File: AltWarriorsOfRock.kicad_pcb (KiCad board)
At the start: 2 copper layers, 33 x 90.5 mm, 40 parts, among them J1 Fret Board, J2 PM20205HBDN, J3 PM20203HBDN, J4 USB4930-00-A_REVA, J5 Debug, SW3 1825910-6, SW4 1825910-6, U1 ESP32-S3-WROOM-1, U2 AMS1117-3.3

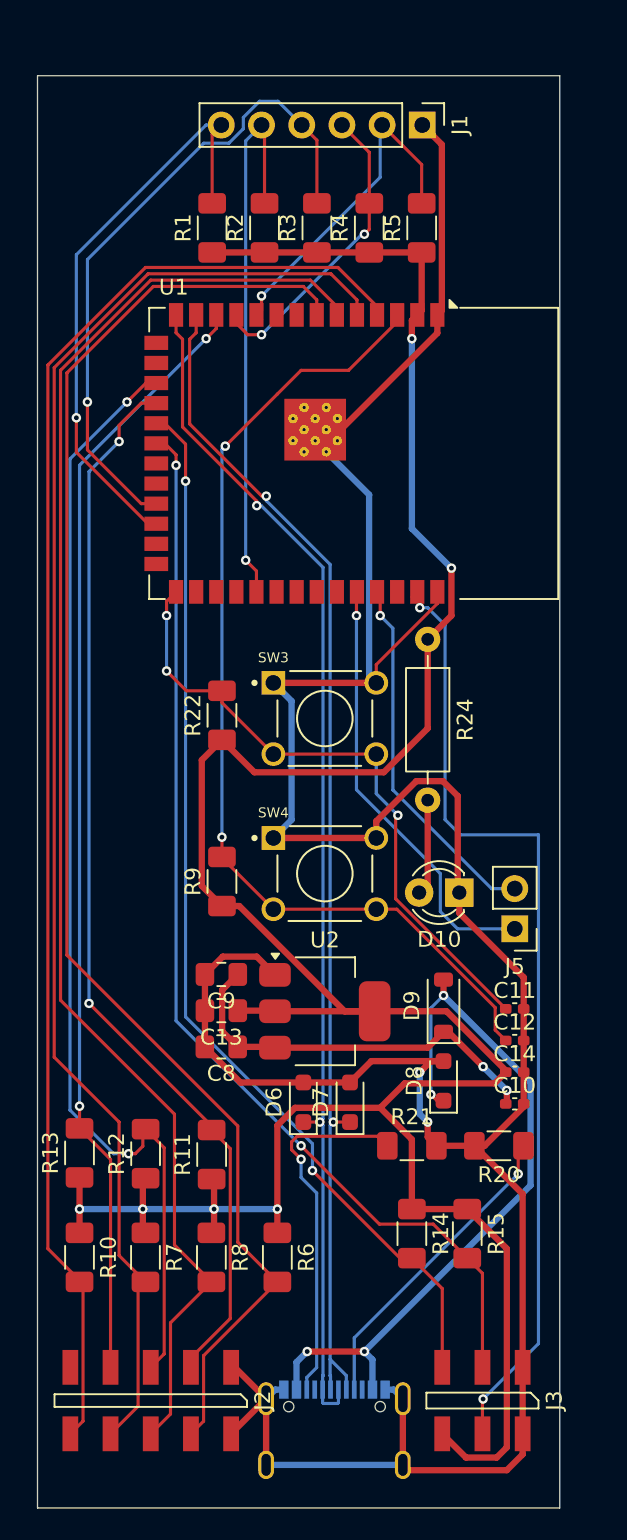
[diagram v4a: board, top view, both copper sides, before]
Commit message: Redo layout with all components topside
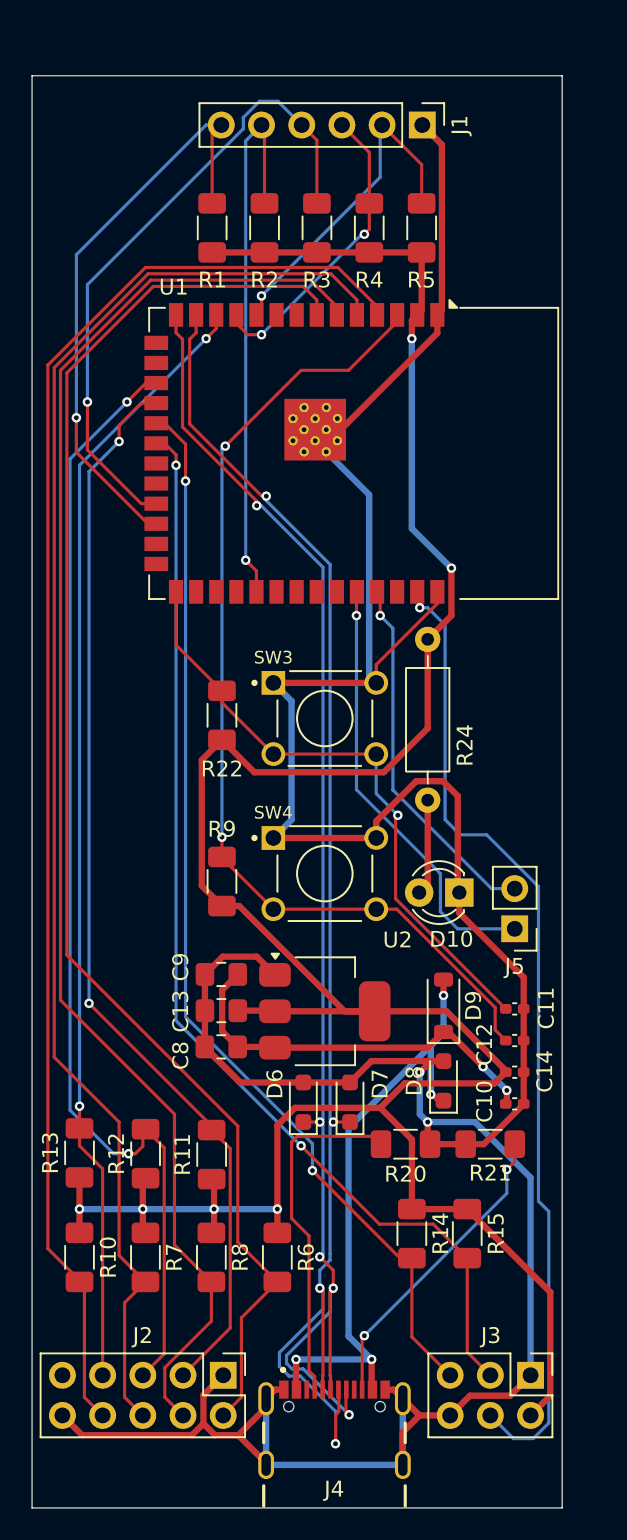
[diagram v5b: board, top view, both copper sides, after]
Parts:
- J2: value PM20205HBDN -> Misc & D-Pad; footprint Connector_Metz_ygaskh:PM20205HBDN -> Library_ygaskh:PinHeader_2x05_P2.54mm_Vertical_TopBottom
- J3: value PM20203HBDN -> Strum & Whammy; footprint Connector_Metz_ygaskh:PM20203HBDN -> Library_ygaskh:PinHeader_2x03_P2.54mm_Vertical_TopBottom
- J4: moved to F.Cu
- moved R20 5.90 mm to (145.1, 120.9), turned to 0 degrees
- moved R21 4.95 mm to (150.4, 120.9), turned to 180 degrees
- moved J2 4.85 mm to (133.6, 135.5), turned to -90 degrees
- moved J3 3.44 mm to (153.0, 135.5), turned to -90 degrees
- turned J4 to 0 degrees
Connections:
- J2 pad 6: DPad_UP -> DPad_RIGHT
- J2 pad 7: DPad_DOWN -> DPad_LEFT
- J2 pad 8: DPad_LEFT -> DPad_DOWN
- J2 pad 9: DPad_RIGHT -> DPad_UP
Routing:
- net DPad_COM: track 195.4 -> 214.5 mm
- net USB_DN: track 75.5 -> 90.0 mm, vias 2 -> 4
- net USB_DP: track 75.8 -> 86.7 mm, vias 2 -> 5
- net VBUS: track 47.1 -> 39.8 mm
- net Wham_3V3: track 180.3 -> 175.0 mm
- net Net-(J4-CC2): track 23.0 -> 19.5 mm, vias 1 -> 2
- net DPad_RIGHT: track 94.8 -> 92.2 mm
- net Net-(J4-CC1): track 19.8 -> 22.3 mm, vias 1 -> 0
- net GPIO0: track 40.7 -> 38.9 mm, vias 3 -> 1
- net DPad_DOWN: track 93.9 -> 92.8 mm
- net DPad_LEFT: track 93.8 -> 92.7 mm
- net DPad_UP: track 93.7 -> 92.7 mm
- net Fret_Y: track 41.9 -> 40.9 mm
- net Wham_Signal: track 61.5 -> 62.4 mm, vias 2 -> 1
- net Strum_UP: track 67.9 -> 68.6 mm
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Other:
- board size 33 x 90.5 mm -> 33.5 x 90.5 mm

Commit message: Adjust schematic 'no connect' symbols to prevent overlap
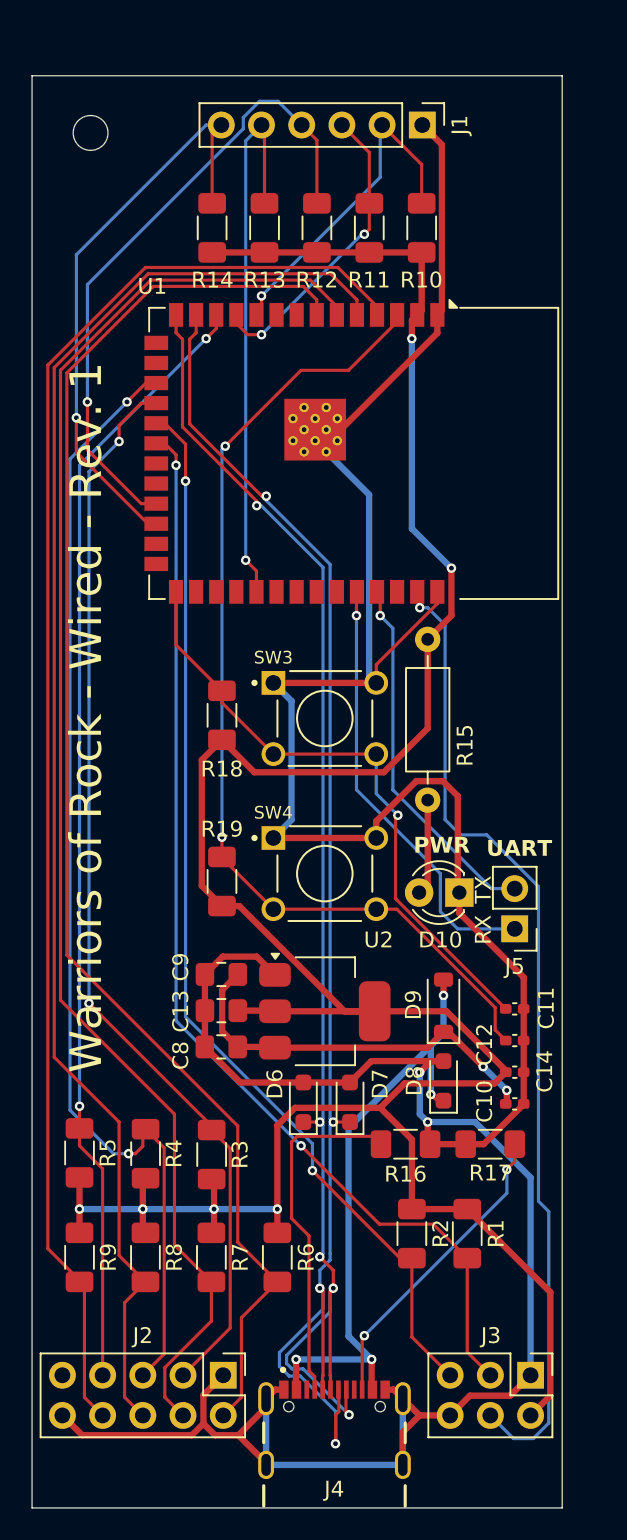
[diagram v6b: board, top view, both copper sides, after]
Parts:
- added REF**: MountingHole_2.2mm_M2, MountingHole:MountingHole_2.2mm_M2, F.Cu at (125.2, 57.0)
- renumbered R15 to R1, R5 to R10, R4 to R11, R3 to R12, R2 to R13, R1 to R14, R24 to R15, R20 to R16, R21 to R17, R22 to R18, R9 to R19, R14 to R2, R11 to R3, R12 to R4, R13 to R5, R8 to R7, R7 to R8, R10 to R9
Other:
- board text added: "PWR"
- board text added: "RX"
- board text added: "TX"
- board text added: "UART"
- board text added: "Warriors of Rock - Wired - Rev. 1"

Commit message: Move C10, C14 closer to respective signals; thickened power/ground traces
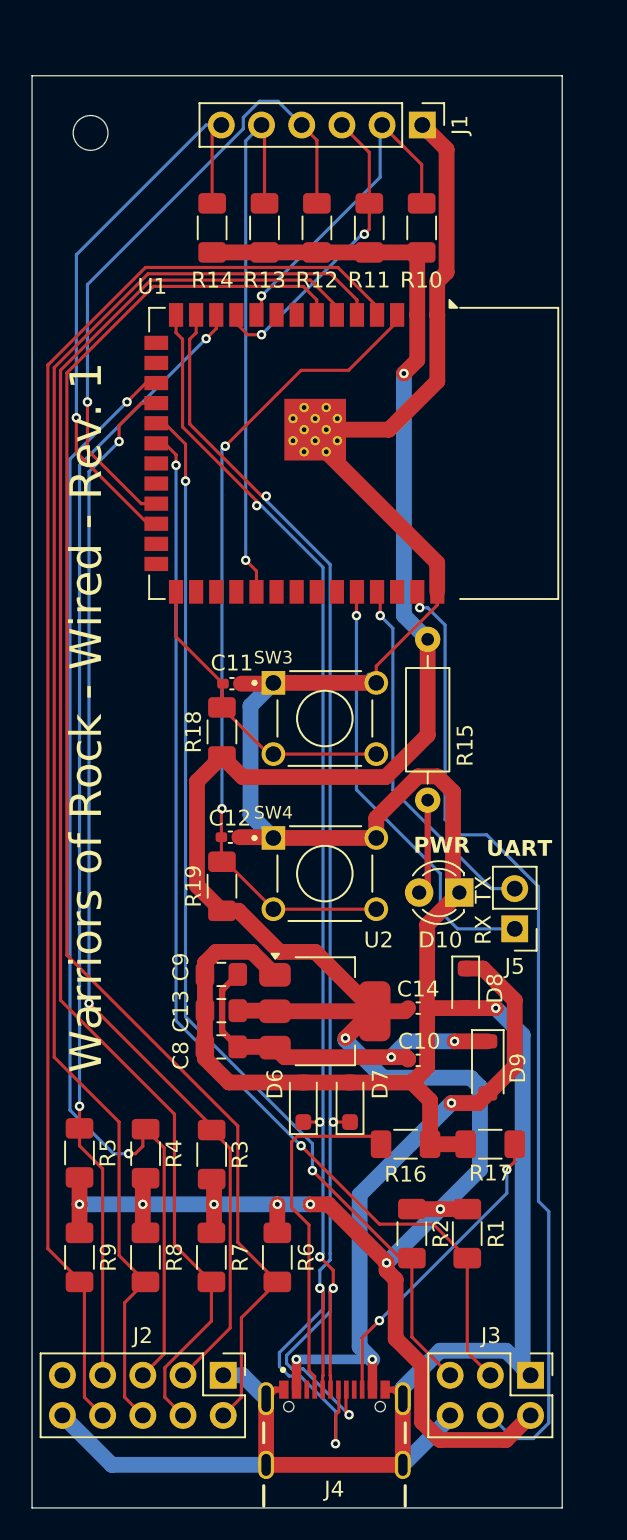
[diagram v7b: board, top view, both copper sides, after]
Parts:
- moved C11 27.2 mm to (134.1, 91.8)
- moved C12 22.1 mm to (134.0, 101.5)
- moved C14 7.32 mm to (145.9, 112.3)
- moved C10 6.69 mm to (145.9, 115.6)
- moved D8 6.02 mm to (148.9, 111.0), turned to -90 degrees
- moved D9 4.80 mm to (150.3, 116.0), turned to -90 degrees
- moved R18 1.05 mm to (133.5, 94.8)
- moved R19 0.30 mm to (133.5, 104.6)
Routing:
- net GPIO0: track 38.9 -> 19.5 mm, vias 1 -> 0
- net ESP_EN: track 64.2 -> 51.9 mm
- net +5V: track 25.2 -> 23.0 mm
- net DPad_COM: track 214.5 -> 216.0 mm, vias 2 -> 1
- net Wham_3V3: track 175.0 -> 176.1 mm, vias 6 -> 9
- net VBUS: track 39.8 -> 40.7 mm, vias 4 -> 3
